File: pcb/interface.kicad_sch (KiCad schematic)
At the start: 13 parts, among them J10 Power Out, J2 QWICC, J5 QWICC, J7 Power In, J9 AVR-UPDI-6, U2 HDC1080, U3 LTR-303ALS-01

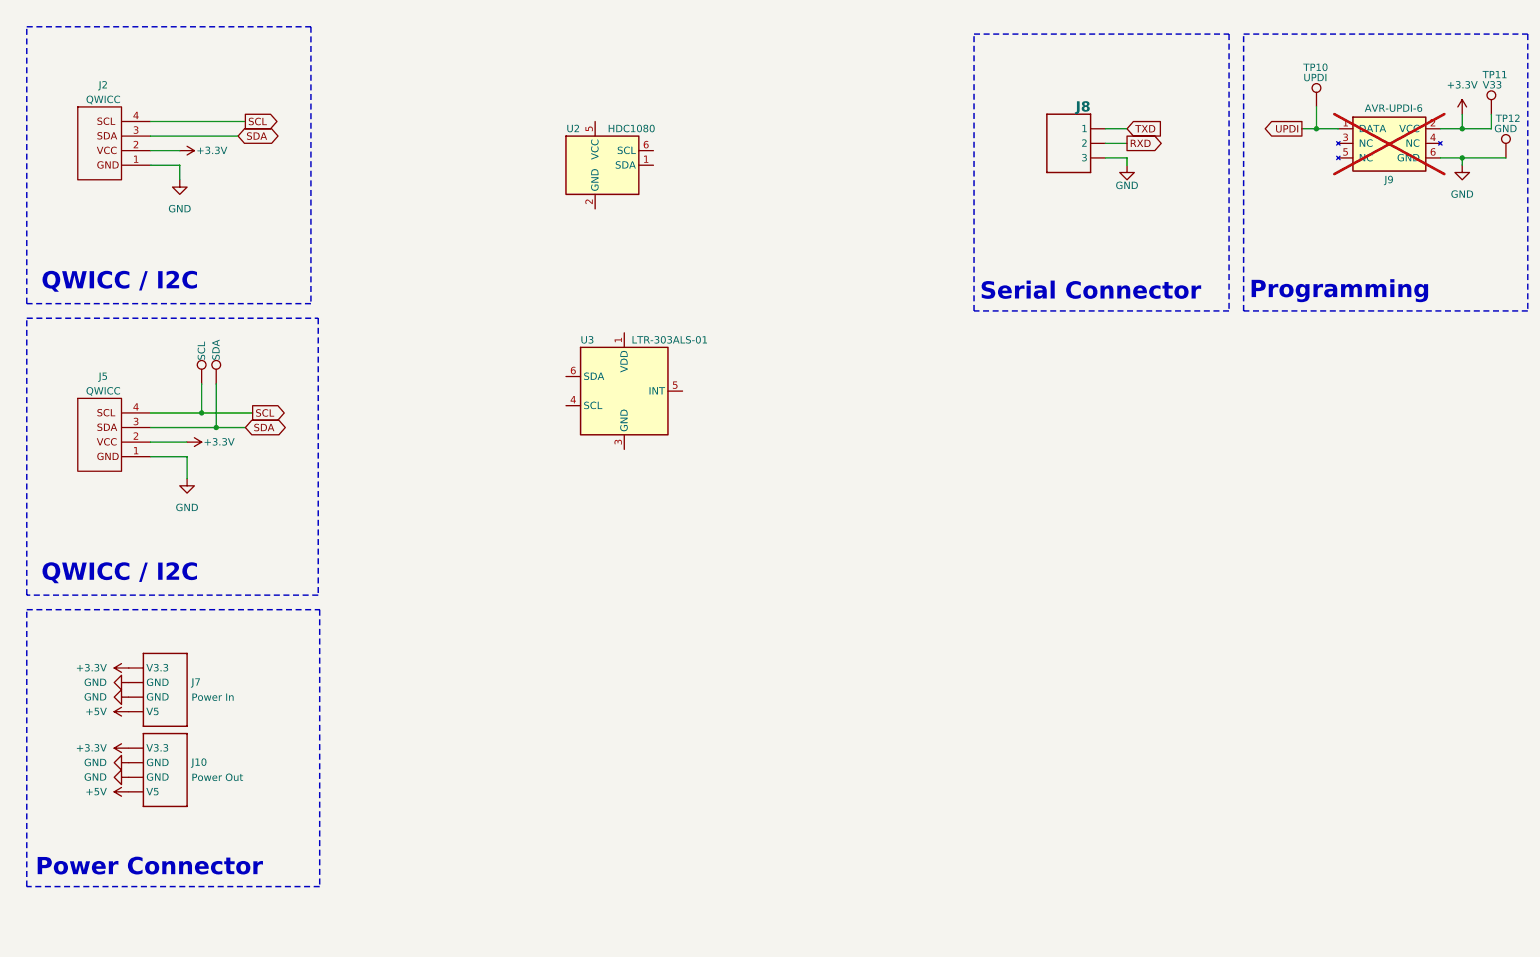
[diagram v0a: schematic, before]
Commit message: Updated license and implemented RP2040
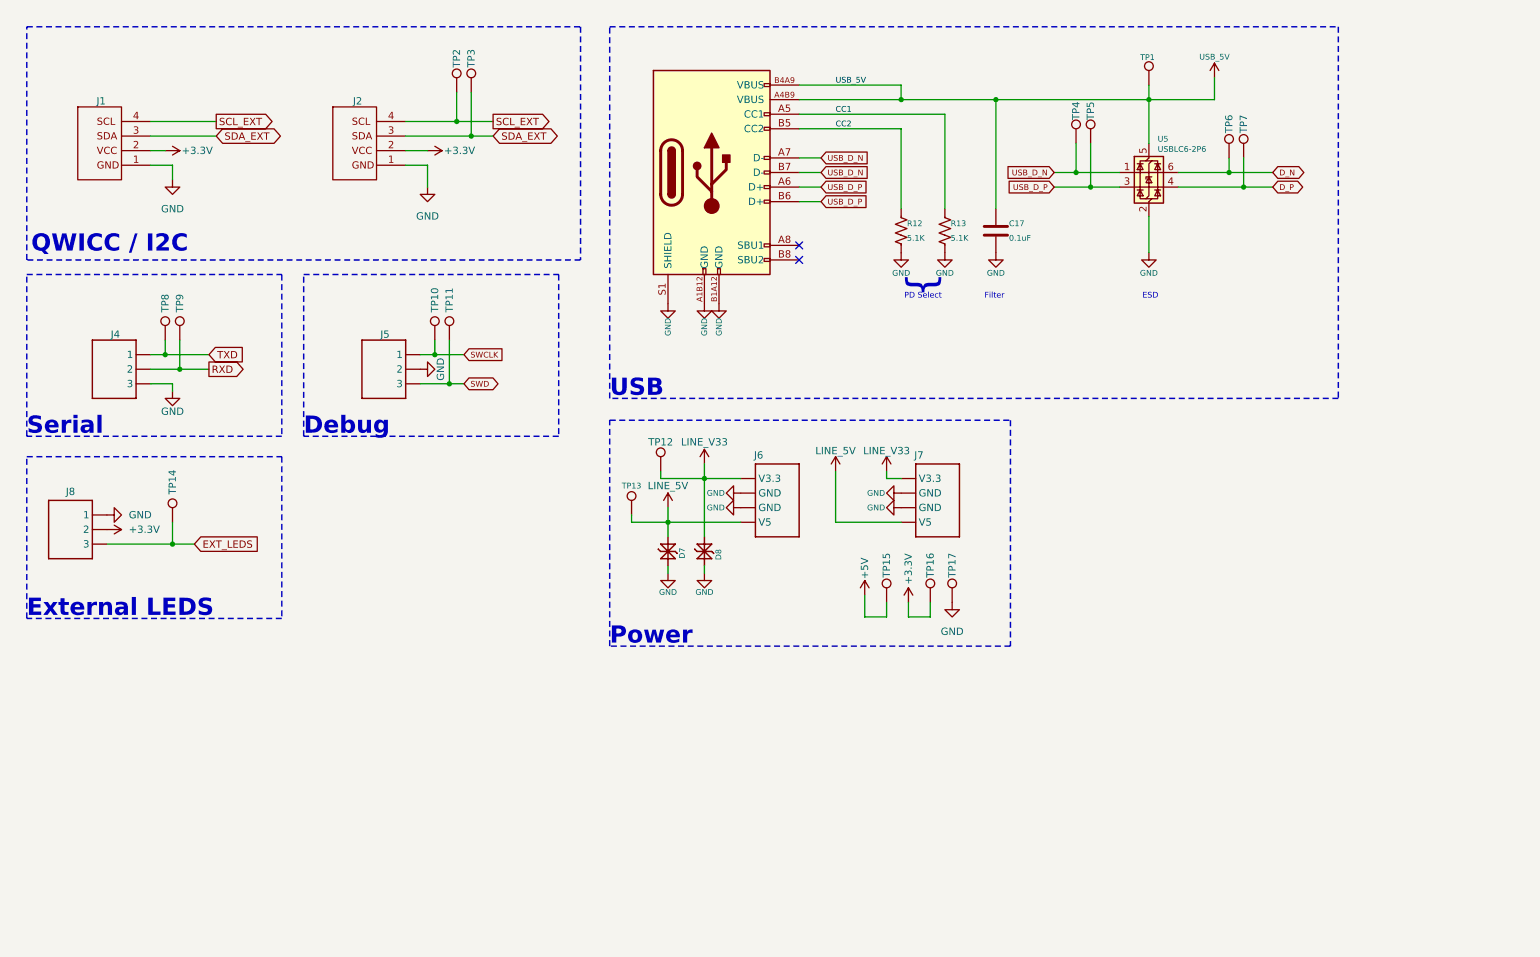
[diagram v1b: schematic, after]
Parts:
- removed J10: Power Out, CRGM Connector:JST_SH_SM04B-SRSS-TB_1x04-1MP_P1.00mm_Horizontal, symbol CRGM Connector:AQ_POWER
- removed J9: AVR-UPDI-6, CRGM Connector:PinHeader_2x03_P2.54mm_Vertical_SMD, symbol CRGM Connector:AVR-UPDI-6
- removed U2: HDC1080, CRG Makes:PWSON-N6, symbol CRG Makes:HDC1080
- removed U3: LTR-303ALS-01, CRG Makes:LTR-303ALS-01, symbol CRG Makes:LTR-303ALS-01
- added C17: 0.1uF, Capacitor_SMD:C_0603_1608Metric, symbol Device:C
- added D7: PESD5V5C1BL, CRGM Passive:DFN1006-2, symbol CRGM Passive:PESD5V5C1BLYL
- added D8: PESD3V3S1BL, CRGM Passive:DFN1006-2, symbol CRGM Passive:PESD3V3S1BL
- added J3: USB_C_USB2.0_16P, CRGM Connector:GCT_USB4105-GF-A, symbol CRGM Connector:USB_C_USB2.0_16P
- added J5: ~, Connector_JST:JST_SH_BM03B-SRSS-TB_1x03-1MP_P1.00mm_Vertical, symbol CRGM Connector:JST-SH-3
- added J7: ~, CRGM Connector:SM04B-SRSS-TB, symbol CRGM Connector:AQ_POWER
- added J8: BM03B-SRSS-TB, Connector_JST:JST_SH_BM03B-SRSS-TB_1x03-1MP_P1.00mm_Vertical, symbol CRGM Connector:JST-SH-3
- added R12, R13: 5.1K, Resistor_SMD:R_0603_1608Metric, symbol Device:R_US
- added TP1, TP12, TP13, TP14, TP15, TP16, TP4, TP5, TP6, TP7, TP8, TP9: ~, CRGM Mechanical:TestPoint_Pad_D1.0mm, symbol Connector:TestPoint
- added U5: USBLC6-2P6, Package_TO_SOT_SMD:SOT-666, symbol Power_Protection:USBLC6-2P6
- J1: renamed from J2; value QWICC -> ~; footprint CRGM Connector:JST_SH_SM04B-SRSS-TB_1x04-1MP_P1.00mm_Horizontal -> CRGM Connector:BM04B-SRSS-TB; Digikey 455-SM04B-SRSS-TBTR-ND -> 455-BM04B-SRSS-TBTR-ND; LCSC C2763614 -> C2919601; MPN SM04B-SRSS-TBT(LF)(SN) -> BM04B-SRSS-TBT(LF)(SN); Mouser 306-SM04BSRSSTBTLFSN -> 306-BM04BSRSSTBTLFSN
- J2: renamed from J5; value QWICC -> ~; footprint CRGM Connector:JST_SH_SM04B-SRSS-TB_1x04-1MP_P1.00mm_Horizontal -> CRGM Connector:BM04B-SRSS-TB; Digikey 455-SM04B-SRSS-TBTR-ND -> 455-BM04B-SRSS-TBTR-ND; LCSC C2763614 -> C2919601; MPN SM04B-SRSS-TBT(LF)(SN) -> BM04B-SRSS-TBT(LF)(SN); Mouser 306-SM04BSRSSTBTLFSN -> 306-BM04BSRSSTBTLFSN
- J4: renamed from J8; footprint CRGM Connector:JST_SH_BM03B-SRSS-TB_1x03-1MP_P1.00mm_Vertical -> Connector_JST:JST_SH_BM03B-SRSS-TB_1x03-1MP_P1.00mm_Vertical
- J6: renamed from J7; value Power In -> ~; footprint CRGM Connector:JST_SH_SM04B-SRSS-TB_1x04-1MP_P1.00mm_Horizontal -> CRGM Connector:SM04B-SRSS-TB
- TP10: value UPDI -> ~
- TP11: value V33 -> ~
- TP17: renamed from TP12; value GND -> ~
- TP2: renamed from TP7; value SCL -> ~
- TP3: renamed from TP8; value SDA -> ~
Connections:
- net +3.3V: now also J8.2, TP16.1; no longer J6.4 (V3.3), TP11.1
- net +5V: now also TP15.1; no longer J6.1 (V5)
- net GND: now also C17.2, D7.1 (K1), D8.1 (K1), J3.A1B12 (GND), J3.B1A12 (GND), J3.S1 (SHIELD), J5.2, J7.2 (GND), J7.3 (GND), J8.1, R12.2, R13.2, U5.2 (GND)
- net RXD: now also TP9.1
- net TXD: now also TP8.1
- net SCL renamed SCL_EXT
- net SDA renamed SDA_EXT
- net UPDI renamed SWCLK
- net SWCLK: now also J5.1
- new net CC1: J3.A5 (CC1), R13.1
- new net CC2: J3.B5 (CC2), R12.1
- new net D_N: TP6.1, U5.6 (I/O1)
- new net D_P: TP7.1, U5.4 (I/O2)
- new net EXT_LEDS: J8.3, TP14.1
- new net LINE_5V: D7.2 (K2), J6.1 (V5), J7.1 (V5), TP13.1
- new net LINE_V33: D8.2 (K2), J6.4 (V3.3), J7.4 (V3.3), TP12.1
- new net SWD: J5.3, TP11.1
- new net USB_5V: C17.1, J3.A4B9 (VBUS), J3.B4A9 (VBUS), TP1.1, U5.5 (VBUS)
- new net USB_D_N: J3.A7 (D-), J3.B7 (D-), TP4.1, U5.1 (I/O1)
- new net USB_D_P: J3.A6 (D+), J3.B6 (D+), TP5.1, U5.3 (I/O2)
- no-connect marks 0 -> 2
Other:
- note added: "Debug"
- note added: "ESD"
- note added: "External LEDS"
- note added: "Filter"
- note added: "PD Select"
- note added: "Power"
- note added: "Serial"
- note added: "USB"
- note added: "{"
- note removed: "Power Connector"
- note removed: "Programming"
- note removed: "Serial Connector"
- moved on the sheet: J2, J4, J6, TP17

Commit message: Added interfaces and fully routed PCB
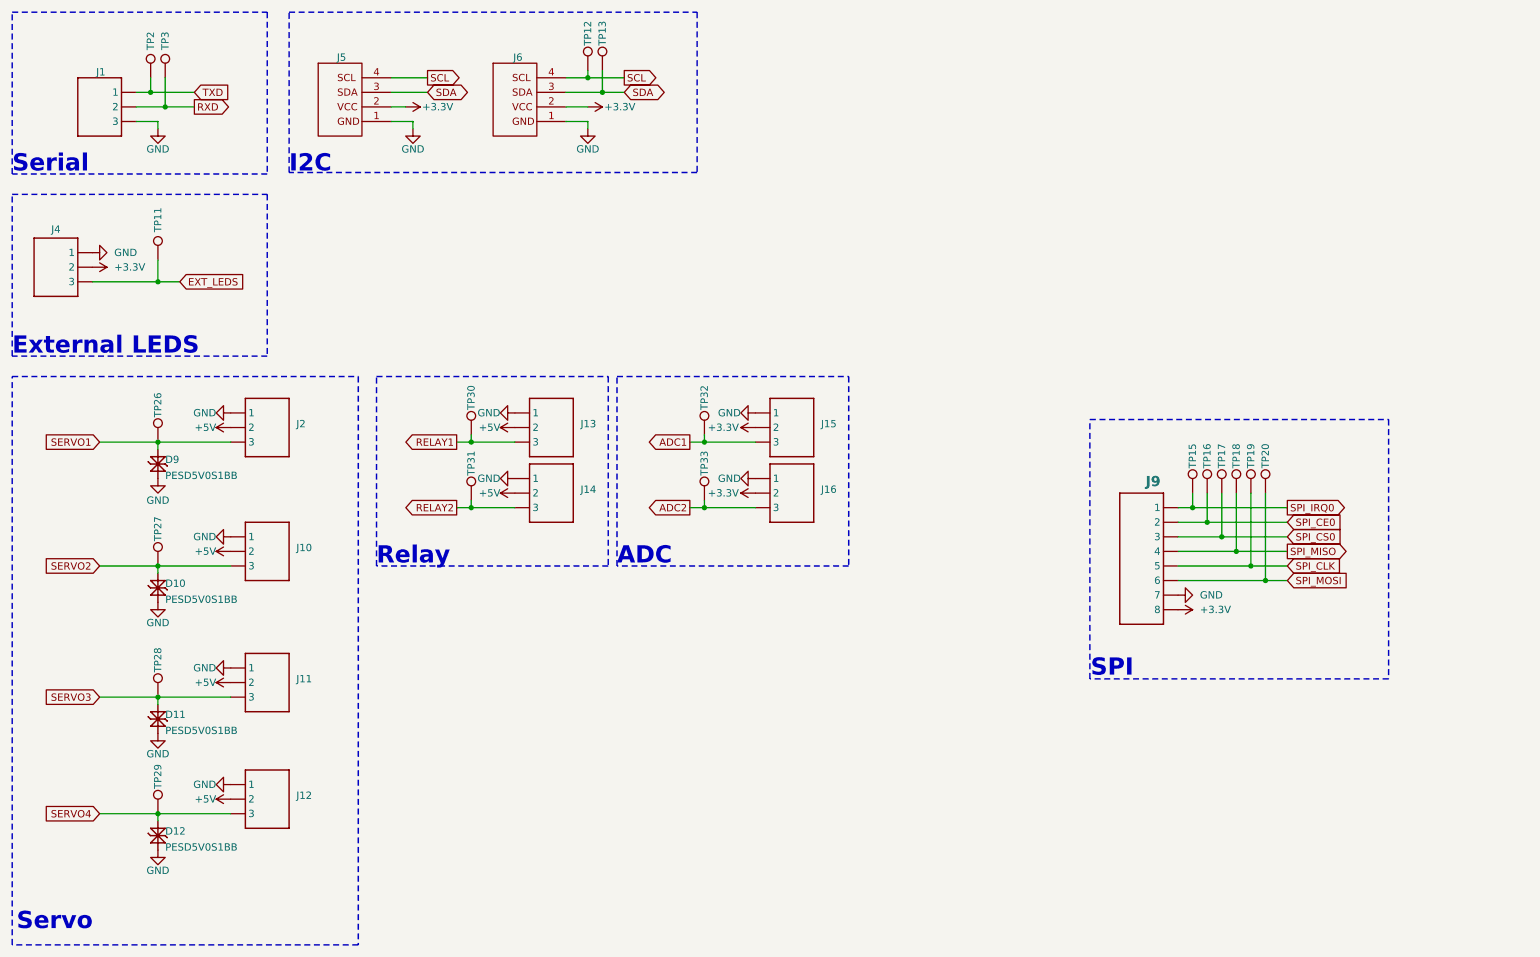
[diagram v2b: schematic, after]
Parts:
- removed C17: 0.1uF, Capacitor_SMD:C_0603_1608Metric, symbol Device:C
- removed D7: PESD5V5C1BL, CRGM Passive:DFN1006-2, symbol CRGM Passive:PESD5V5C1BLYL
- removed D8: PESD3V3S1BL, CRGM Passive:DFN1006-2, symbol CRGM Passive:PESD3V3S1BL
- removed J3: USB_C_USB2.0_16P, CRGM Connector:GCT_USB4105-GF-A, symbol CRGM Connector:USB_C_USB2.0_16P
- removed J5: ~, Connector_JST:JST_SH_BM03B-SRSS-TB_1x03-1MP_P1.00mm_Vertical, symbol CRGM Connector:JST-SH-3
- removed J6, J7: ~, CRGM Connector:SM04B-SRSS-TB, symbol CRGM Connector:AQ_POWER
- removed R12, R13: 5.1K, Resistor_SMD:R_0603_1608Metric, symbol Device:R_US
- removed TP1, TP10, TP11, TP12, TP13, TP4, TP5, TP6, TP7: ~, CRGM Mechanical:TestPoint_Pad_D1.0mm, symbol Connector:TestPoint
- removed U5: USBLC6-2P6, Package_TO_SOT_SMD:SOT-666, symbol Power_Protection:USBLC6-2P6
- added D10, D11, D12, D9: PESD5V0S1BB, CRGM Passive:D_SOD-523, symbol CRGM Passive:PESD5V0S1BB
- added J10, J11, J12, J13, J14, J15, J16, J2: ~, CRGM Connector:JST_SH_BM03B-SRSS-TB_1x03-1MP_P1.00mm_Vertical, symbol CRGM Connector:JST-SH-3
- added J9: BM08B-SRSS-TB, CRGM Connector:JST_SH_BM08B-SRSS-TB_1x08-1MP_P1.00mm_Vertical, symbol CRGM Connector:JST-SH-8
- added TP18, TP19, TP20, TP26, TP27, TP28, TP29, TP30, TP31, TP32, TP33: ~, CRGM Mechanical:TestPoint_Pad_D1.0mm, symbol Connector:TestPoint
- J1: renamed from J4; footprint Connector_JST:JST_SH_BM03B-SRSS-TB_1x03-1MP_P1.00mm_Vertical -> CRGM Connector:JST_SH_BM03B-SRSS-TB_1x03-1MP_P1.00mm_Vertical
- J4: renamed from J8; footprint Connector_JST:JST_SH_BM03B-SRSS-TB_1x03-1MP_P1.00mm_Vertical -> CRGM Connector:JST_SH_BM03B-SRSS-TB_1x03-1MP_P1.00mm_Vertical
- J5: renamed from J1; footprint CRGM Connector:BM04B-SRSS-TB -> CRGM Connector:JST_SH_BM04B-SRSS-TB_1x04-1MP_P1.00mm_Vertical
- J6: renamed from J2; footprint CRGM Connector:BM04B-SRSS-TB -> CRGM Connector:JST_SH_BM04B-SRSS-TB_1x04-1MP_P1.00mm_Vertical
- renumbered TP14 to TP11, TP2 to TP12, TP3 to TP13, TP8 to TP2, TP9 to TP3
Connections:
- net +3.3V: now also J15.2, J16.2, J9.8; no longer TP16.1
- net +5V: now also J10.2, J11.2, J12.2, J13.2, J14.2, J2.2; no longer TP15.1
- net GND: now also D10.1 (K1), D11.1 (K1), D12.1 (K1), D9.1 (K1), J10.1, J11.1, J12.1, J13.1, J14.1, J15.1, J16.1, J2.1, J9.7; no longer TP17.1
- net SCL_EXT renamed SCL
- net SDA_EXT renamed SDA
- new net ADC1: J15.3, TP32.1
- new net ADC2: J16.3, TP33.1
- new net RELAY1: J13.3, TP30.1
- new net RELAY2: J14.3, TP31.1
- new net SERVO1: D9.2 (K2), J2.3, TP26.1
- new net SERVO2: D10.2 (K2), J10.3, TP27.1
- new net SERVO3: D11.2 (K2), J11.3, TP28.1
- new net SERVO4: D12.2 (K2), J12.3, TP29.1
- new net SPI_CE0: J9.2, TP16.1
- new net SPI_CLK: J9.5, TP19.1
- new net SPI_CS0: J9.3, TP17.1
- new net SPI_IRQ0: J9.1, TP15.1
- new net SPI_MISO: J9.4, TP18.1
- new net SPI_MOSI: J9.6, TP20.1
- no-connect marks 2 -> 0
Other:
- note added: "ADC"
- note added: "I2C"
- note added: "Relay"
- note added: "SPI"
- note added: "Servo"
- note removed: "Debug"
- note removed: "ESD"
- note removed: "Filter"
- note removed: "PD Select"
- note removed: "Power"
- note removed: "QWICC / I2C"
- note removed: "USB"
- note removed: "{"
- moved on the sheet: J1, J4, J5, J6, TP11, TP12, TP13, TP2, TP3

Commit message: Change schematic name
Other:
- title: Environment Module -> Client
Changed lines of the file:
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@@
 	(paper "A4")
 	(title_block
-		(title "Environment Module")
+		(title "Client")
 		(date "<<release-date>>")
 		(rev "<<tag>>")
@@
 			)
 		)
-		(property "Description" "JST SH 1.0mm 8 Position Vertical"
+		(property "Description" "8 position, 1mm connector"
 			(at 215.9 99.06 0)
 			(effects

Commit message: Updated project name and properties
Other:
- title: Client -> Client Hardware
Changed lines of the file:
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@@
 	(paper "A4")
 	(title_block
-		(title "Client")
+		(title "Client Hardware")
 		(date "<<release-date>>")
 		(rev "<<tag>>")
@@
 	(rectangle
 		(start 15.24 78.74)
-		(end 75.565 177.8)
+		(end 75.565 168.148)
 		(stroke
 			(width 0.254)
@@
 	(text "Servo"
 		(exclude_from_sim no)
-		(at 16.002 173.736 0)
+		(at 15.24 168.148 0)
 		(effects
 			(font
@@
 				(bold yes)
 			)
-			(justify left)
+			(justify left bottom)
 		)
 	)

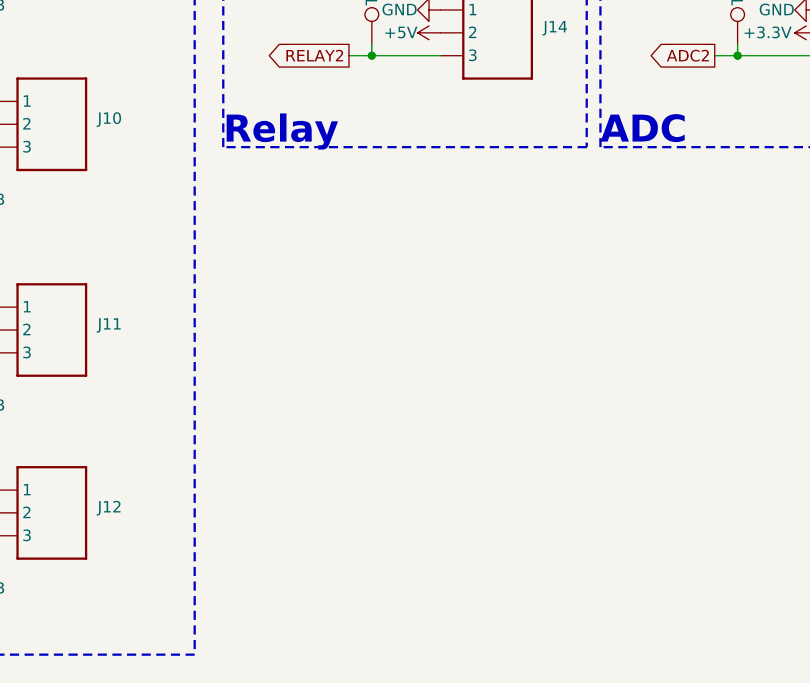
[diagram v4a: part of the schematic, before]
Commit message: Added button inputs and pull ups
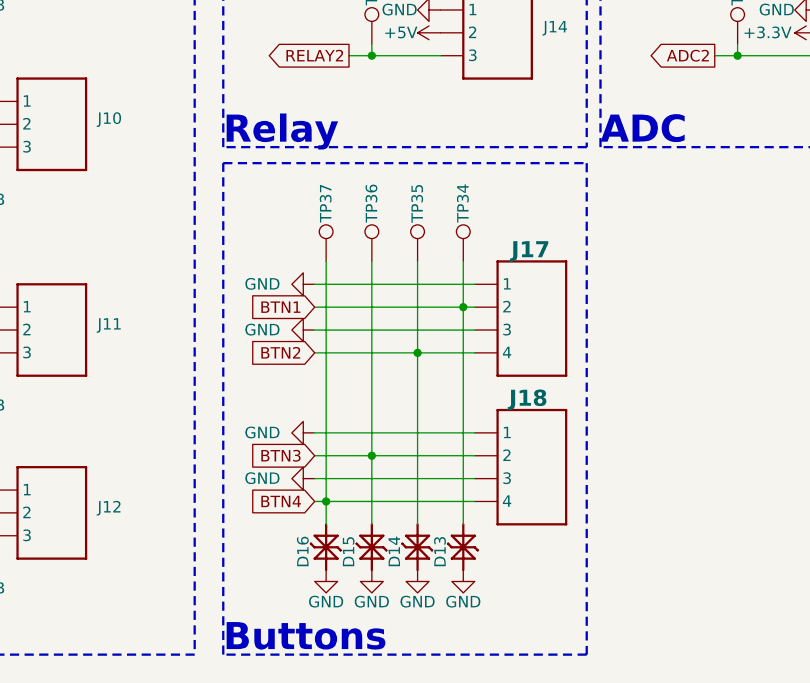
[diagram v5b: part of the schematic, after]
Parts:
- added D13, D14, D15, D16: PESD5V0S1BB, CRGM Passive:D_SOD-523, symbol CRGM Passive:PESD5V0S1BB
- added J17, J18: BM04B-SRSS-TB, CRGM Connector:JST_SH_BM04B-SRSS-TB_1x04-1MP_P1.00mm_Vertical, symbol CRGM Connector:JST-SH-4
- added TP34, TP35, TP36, TP37: ~, CRGM Mechanical:TestPoint_Pad_D1.0mm, symbol Connector:TestPoint
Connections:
- net GND: now also D13.1 (K1), D14.1 (K1), D15.1 (K1), D16.1 (K1), J17.1, J17.3, J18.1, J18.3
- new net BTN1: D13.2 (K2), J17.2, TP34.1
- new net BTN2: D14.2 (K2), J17.4, TP35.1
- new net BTN3: D15.2 (K2), J18.2, TP36.1
- new net BTN4: D16.2 (K2), J18.4, TP37.1
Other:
- note added: "Buttons"
